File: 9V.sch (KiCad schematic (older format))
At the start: 14 parts

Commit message: Boost converter completed
All values are calculated
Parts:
- removed C?: 10µF, symbol C_Small
- removed C? (x2): 0.1µF, symbol C_Small
- removed C?: 2.2µF, symbol C_Small
- removed C?: C7, symbol C_Small
- removed C?: C5, symbol C_Small
- removed C?: C_Small, symbol C_Small
- removed L?: 1.2µH, symbol L
- removed R?: 255kΩ, symbol R_Small
- removed R?: R4, symbol R_Small
- removed R?: R5, symbol R_Small
- removed R?: R2, symbol R_Small
- removed R?: R1, symbol R_Small
- removed U?: TPS61088, symbol TPS61088-RESCUE-eps_v1
- added Cbsta, Cbstb: 100n, symbol C_Small
- added Ccomp2a, Ccomp2b, Cssa, Cssb: 8.2n, symbol C_Small
- added Ccompa, Ccompb: 1.5n, symbol C_Small
- added Cin2a, Cin2b: 100µ, symbol C_Small
- added Cin3a, Cin3b: 1µ, symbol C_Small
- added Cina, Cinb, Cvcca, Cvccb: 10µ, symbol C_Small
- added Couta, Coutb: 47n, symbol C_Small
- added La, Lb: 5.6µ, symbol L_Small
- added Rcompa, Rcompb: 10.7k, symbol R_Small
- added Rfbba, Rfbbb: 105k, symbol R_Small
- added Rfbta, Rfbtb: 680k, symbol R_Small
- added Rlima, Rlimb: 192k, symbol R_Small
- added Rta, Rtb: 259k, symbol R_Small
- added U? (x2): TPS61088, symbol TPS61088
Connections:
- net labels added: 9VINA, 9VINB, 9VOUTA, 9VOUTB
- net labels removed: 9VIN, 9VOUT, About NC: No connection inside the device. Connect these two pins to ground plane on the PCB for good thermal dissipation, GNDA
- wire segments 36 -> 90
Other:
- note removed: "Finish constructing circuit"

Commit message: SWITCH_3V3
Added emergency switch circuit for 3V3 loads.
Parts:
- removed Cin3b: 1µ, symbol C_Small
- Cin2a, Cin2b: value 100µ -> 100n
- Couta, Coutb: value 47n -> 47µ
- Cvccb: value 10µ -> 1µ
- Rlimb: value 192k -> 102k
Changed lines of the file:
@@
 $Descr A4 11693 8268
 encoding utf-8
-Sheet 5 5
+Sheet 5 6
 Title ""
 Date ""
@@
 P 2400 2700
 F 0 "Cin2a" H 2410 2770 50  0000 L CNN
-F 1 "100µ" H 2410 2620 50  0000 L CNN
+F 1 "100n" H 2410 2620 50  0000 L CNN
 F 2 "" H 2400 2700 50  0001 C CNN
 F 3 "" H 2400 2700 50  0001 C CNN
@@
 P 7300 3000
 F 0 "Couta" H 7310 3070 50  0000 L CNN
-F 1 "47n" H 7310 2920 50  0000 L CNN
+F 1 "47µ" H 7310 2920 50  0000 L CNN
 F 2 "" H 7300 3000 50  0001 C CNN
 F 3 "" H 7300 3000 50  0001 C CNN
@@
 P 2400 5400
 F 0 "Cin2b" H 2410 5470 50  0000 L CNN
-F 1 "100µ" H 2410 5320 50  0000 L CNN
+F 1 "100n" H 2410 5320 50  0000 L CNN
 F 2 "" H 2400 5400 50  0001 C CNN
 F 3 "" H 2400 5400 50  0001 C CNN
 	1    2400 5400
-	1    0    0    -1
-$EndComp
-$Comp
-L C_Small Cin3b
-U 1 1 5A1A42B3
-P 2700 5400
-F 0 "Cin3b" H 2710 5470 50  0000 L CNN
-F 1 "1µ" H 2710 5320 50  0000 L CNN
-F 2 "" H 2700 5400 50  0001 C CNN
-F 3 "" H 2700 5400 50  0001 C CNN
-	1    2700 5400
 	1    0    0    -1
 $EndComp
@@
 P 3000 5400
 F 0 "Cvccb" H 3010 5470 50  0000 L CNN
-F 1 "10µ" H 3010 5320 50  0000 L CNN
+F 1 "1µ" H 3010 5320 50  0000 L CNN
 F 2 "" H 3000 5400 50  0001 C CNN
 F 3 "" H 3000 5400 50  0001 C CNN
@@
 P 3900 5650
 F 0 "Rlimb" H 3930 5670 50  0000 L CNN
-F 1 "192k" H 3930 5610 50  0000 L CNN
+F 1 "102k" H 3930 5610 50  0000 L CNN
 F 2 "" H 3900 5650 50  0001 C CNN
 F 3 "" H 3900 5650 50  0001 C CNN
@@
 Connection ~ 2400 4600
 Wire Wire Line
-	2700 5300 2700 4600
-Connection ~ 2700 4600
-Wire Wire Line
 	2400 5500 2400 6200
 Connection ~ 2400 6200
-Wire Wire Line
-	2700 5500 2700 6200
 Connection ~ 2700 6200
 Wire Wire Line
@@
 P 7300 5700
 F 0 "Coutb" H 7310 5770 50  0000 L CNN
-F 1 "47n" H 7310 5620 50  0000 L CNN
+F 1 "47µ" H 7310 5620 50  0000 L CNN
 F 2 "" H 7300 5700 50  0001 C CNN
 F 3 "" H 7300 5700 50  0001 C CNN

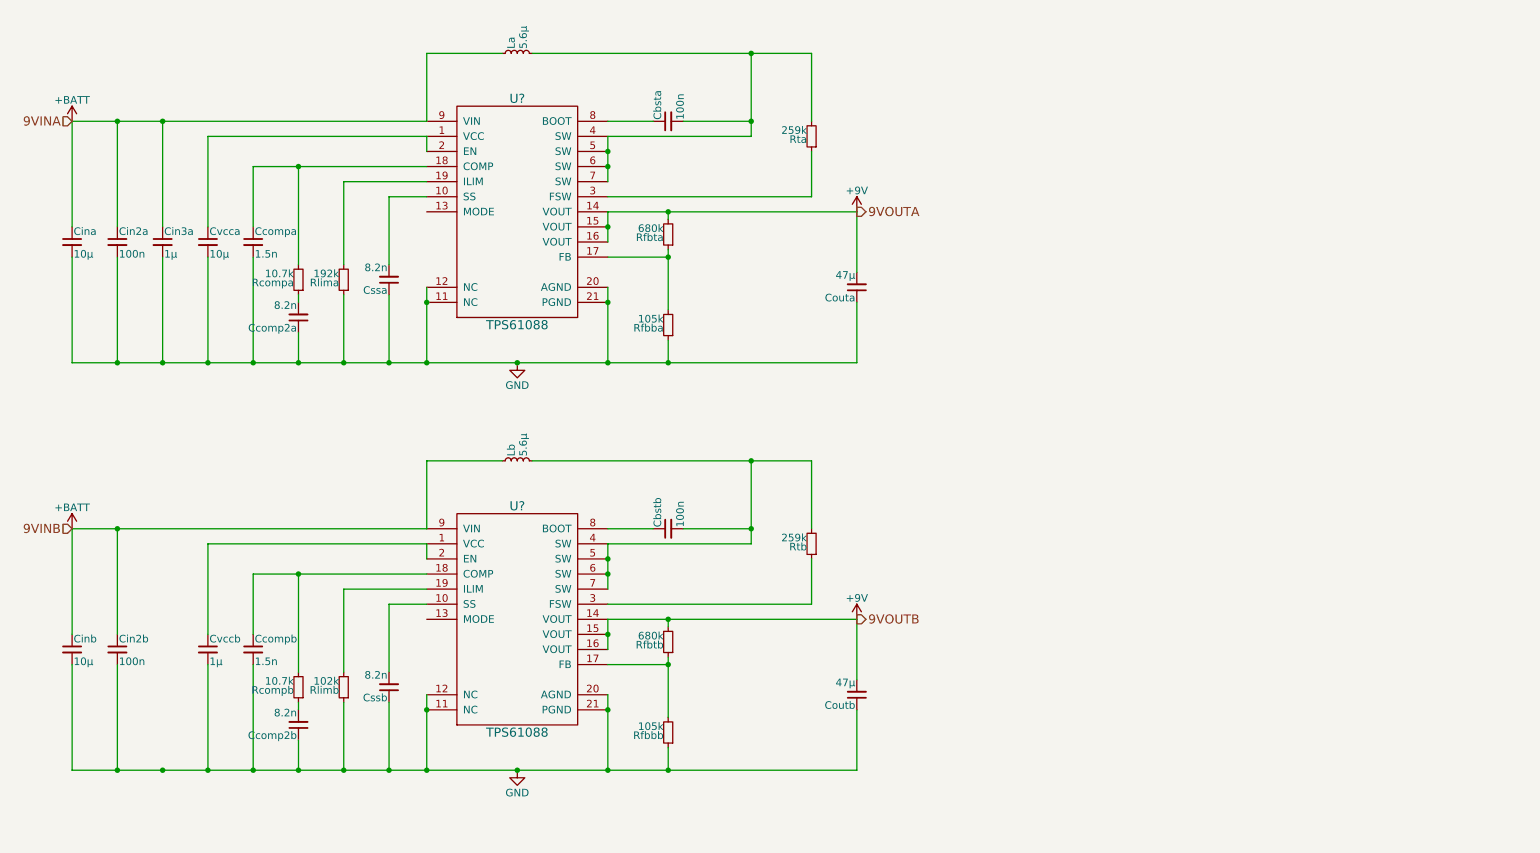
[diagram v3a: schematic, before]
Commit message: Voltmeters added to 3V3 and 9V
Added 4 voltmeters. Outputs still need to be added to hierarchical sheets.
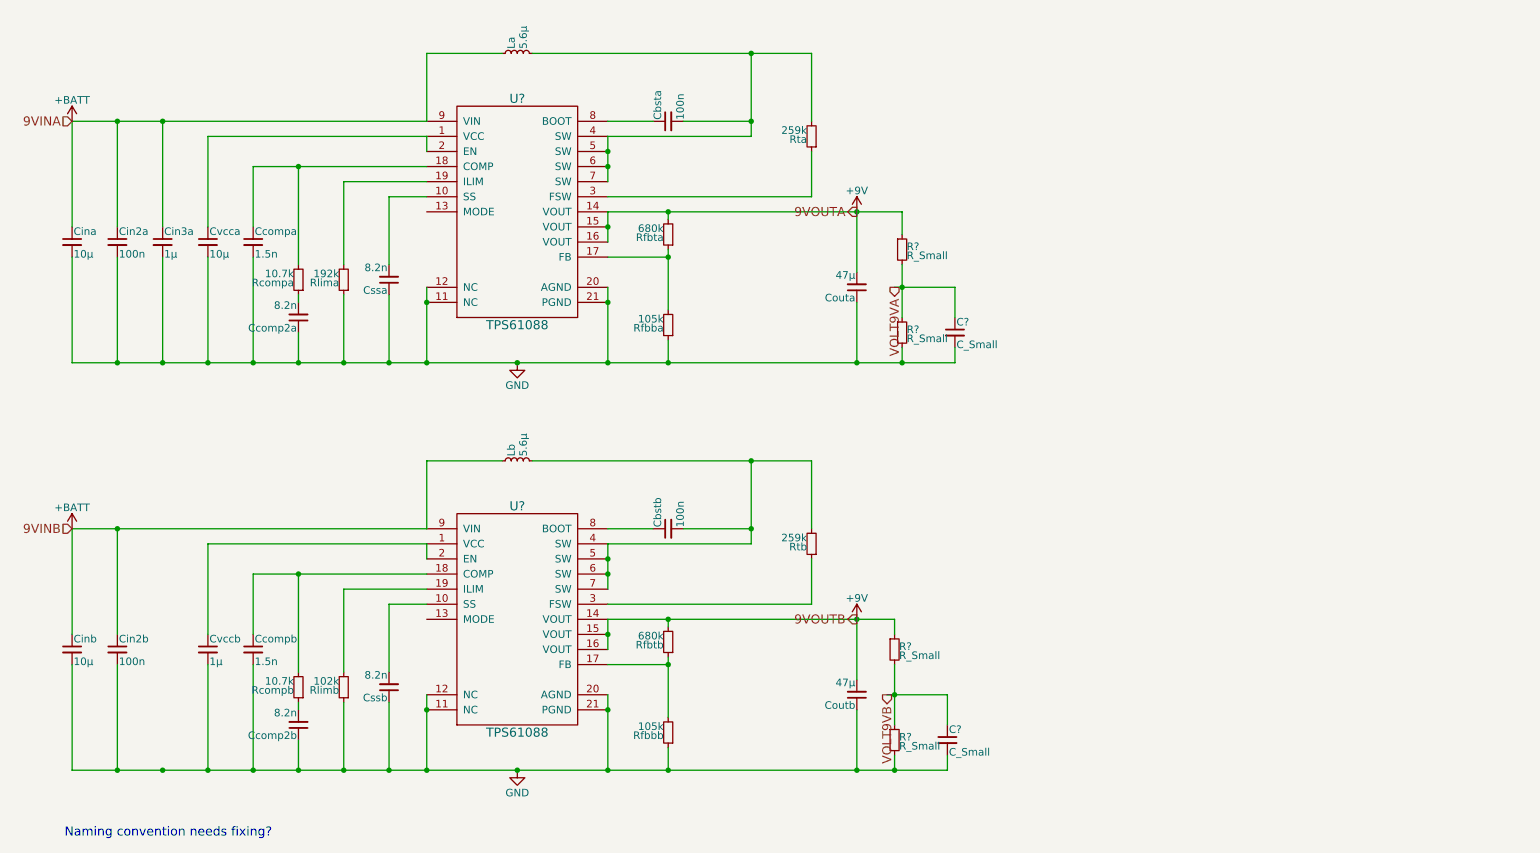
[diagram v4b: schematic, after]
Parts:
- added C? (x2): C_Small, symbol C_Small
- added R? (x4): R_Small, symbol R_Small
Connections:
- net +9V: now also R?.1, R?.1
- net GND: now also C?.2, C?.2, R?.2, R?.2
- new net VOLT9VA: C?.1, R?.1, R?.2
- new net VOLT9VB: C?.1, R?.1, R?.2
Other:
- note added: "Naming convention needs fixing?"
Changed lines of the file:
@@
 	1    0    0    -1
 $EndComp
-Text HLabel 7300 2500 2    60   Output ~ 0
+Text HLabel 7300 2500 0    60   Output ~ 0
 9VOUTA
 Text HLabel 2100 1900 0    60   Input ~ 0
@@
 	3000 2000 3000 2600
 Wire Wire Line
-	2100 3500 7300 3500
+	2100 3500 7950 3500
 Wire Wire Line
 	2400 2600 2400 1900
@@
 	6050 2550 6050 2500
 Wire Wire Line
-	5650 2500 7300 2500
+	5650 2500 7600 2500
 Wire Wire Line
 	6050 2750 6050 3150
@@
 	1    0    0    -1
 $EndComp
-Text HLabel 7300 5200 2    60   Output ~ 0
-9VOUTB
 Text HLabel 2100 4600 0    60   Input ~ 0
 9VINB
@@
 	3000 4700 3000 5300
 Wire Wire Line
-	2100 6200 7300 6200
+	2100 6200 7900 6200
 Wire Wire Line
 	2400 5300 2400 4600
@@
 	6050 5250 6050 5200
 Wire Wire Line
-	5650 5200 7300 5200
+	5650 5200 7550 5200
 Wire Wire Line
 	6050 5450 6050 5850
@@
 	7300 6200 7300 5800
 Connection ~ 6050 6200
+Text HLabel 7300 5200 0    60   Output ~ 0
+9VOUTB
+Wire Wire Line
+	7550 5200 7550 5300
+Connection ~ 7300 5200
+$Comp
+L R_Small R?
+U 1 1 5A277DE7
+P 7550 5400
+F 0 "R?" H 7580 5420 50  0000 L CNN
+F 1 "R_Small" H 7580 5360 50  0000 L CNN
+F 2 "" H 7550 5400 50  0001 C CNN
+F 3 "" H 7550 5400 50  0001 C CNN
+	1    7550 5400
+	1    0    0    -1
+$EndComp
+$Comp
+L R_Small R?
+U 1 1 5A277E75
+P 7550 6000
+F 0 "R?" H 7580 6020 50  0000 L CNN
+F 1 "R_Small" H 7580 5960 50  0000 L CNN
+F 2 "" H 7550 6000 50  0001 C CNN
+F 3 "" H 7550 6000 50  0001 C CNN
+	1    7550 6000
+	1    0    0    -1
+$EndComp
+$Comp
+L C_Small C?
+U 1 1 5A277EF3
+P 7900 6000
+F 0 "C?" H 7910 6070 50  0000 L CNN
+F 1 "C_Small" H 7910 5920 50  0000 L CNN
+F 2 "" H 7900 6000 50  0001 C CNN
+F 3 "" H 7900 6000 50  0001 C CNN
+	1    7900 6000
+	1    0    0    -1
+$EndComp
+Wire Wire Line
+	7550 5500 7550 5900
+Wire Wire Line
+	7900 5700 7900 5900
+Wire Wire Line
+	7500 5700 7900 5700
+Connection ~ 7550 5700
+Wire Wire Line
+	7550 6200 7550 6100
+Connection ~ 7300 6200
+Text HLabel 7500 5700 3    60   Output ~ 0
+VOLT9VB
+Wire Wire Line
+	7900 6200 7900 6100
+Connection ~ 7550 6200
+Wire Wire Line
+	7600 2500 7600 2650
+Connection ~ 7300 2500
+$Comp
+L C_Small C?
+U 1 1 5A27979D
+P 7950 3300
+F 0 "C?" H 7960 3370 50  0000 L CNN
+F 1 "C_Small" H 7960 3220 50  0000 L CNN
+F 2 "" H 7950 3300 50  0001 C CNN
+F 3 "" H 7950 3300 50  0001 C CNN
+	1    7950 3300
+	1    0    0    -1
+$EndComp
+$Comp
+L R_Small R?
+U 1 1 5A279826
+P 7600 2750
+F 0 "R?" H 7630 2770 50  0000 L CNN
+F 1 "R_Small" H 7630 2710 50  0000 L CNN
+F 2 "" H 7600 2750 50  0001 C CNN
+F 3 "" H 7600 2750 50  0001 C CNN
+	1    7600 2750
+	1    0    0    -1
+$EndComp
+$Comp
+L R_Small R?
+U 1 1 5A2798A7
+P 7600 3300
+F 0 "R?" H 7630 3320 50  0000 L CNN
+F 1 "R_Small" H 7630 3260 50  0000 L CNN
+F 2 "" H 7600 3300 50  0001 C CNN
+F 3 "" H 7600 3300 50  0001 C CNN
+	1    7600 3300
+	1    0    0    -1
+$EndComp
+Wire Wire Line
+	7600 2850 7600 3200
+Wire Wire Line
+	7550 3000 7950 3000
+Wire Wire Line
+	7950 3000 7950 3200
+Connection ~ 7600 3000
+Wire Wire Line
+	7600 3500 7600 3400
+Connection ~ 7300 3500
+Wire Wire Line
+	7950 3500 7950 3400
+Connection ~ 7600 3500
+Text HLabel 7550 3000 3    60   Output ~ 0
+VOLT9VA
+Text Notes 2050 6650 0    60   ~ 0
+Naming convention needs fixing?
 $EndSCHEMATC
